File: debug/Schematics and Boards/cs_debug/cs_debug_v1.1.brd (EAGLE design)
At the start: 81.5 x 62.2 mm, 217 parts, among them J1 J-JTAG-CORTEX_SMD, J19 Solar, J3 HIROSE-DF40_50-PIN_CONNECTORS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, J5 J-WURTH-USBC, Q10 2N7002P, Q3 FDN340P, Q4 2N7002P, Q5 FDN340P, Q6 2N7002P, Q7 FDN340P, Q8 2N7002P, Q9 FDN340P, U1 AP2120N-3.3TRG1, U10 OPA357AIDBVTG4, U11 DAC7574IDGS, U12 MCP73871T-2CCI/ML, U13 USB2412-DZK, U14 INA225AIDGK, U15 OPA357AIDBVTG4, U2 TLV1117LV33DCYR, U204 LOADSWITCH-MIC94164, U3 ESD122DMYR, U5 INA225AIDGK, U6 OPA357AIDBVTG4, U7 INA225AIDGK, U8 OPA357AIDBVTG4, U9 INA225AIDGK, Y1 EPSON_TSX-3225_24.0000MF10Z-C3, Y101 32.768kHz, Y102 12MHz-12pF-K7

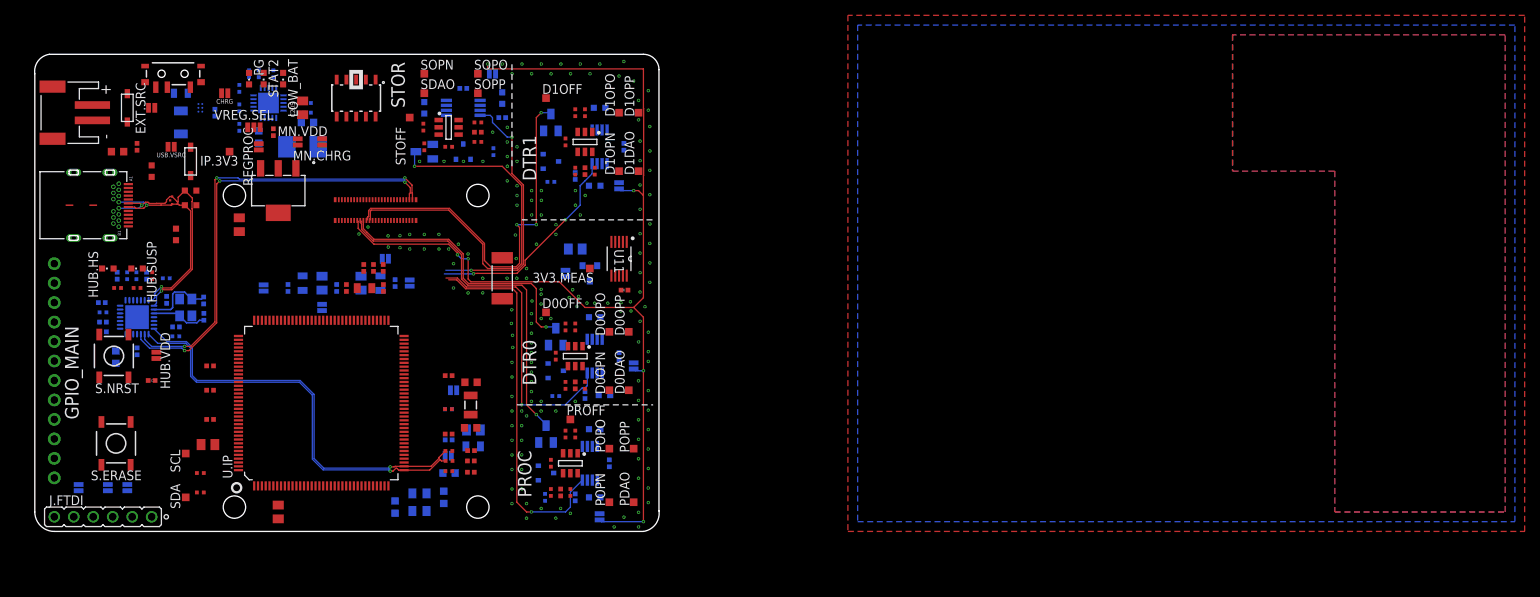
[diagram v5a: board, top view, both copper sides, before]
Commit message: Debug v1.1 board routed w/ 5 mil trace/space, 2 layer, 3.2x2.45in
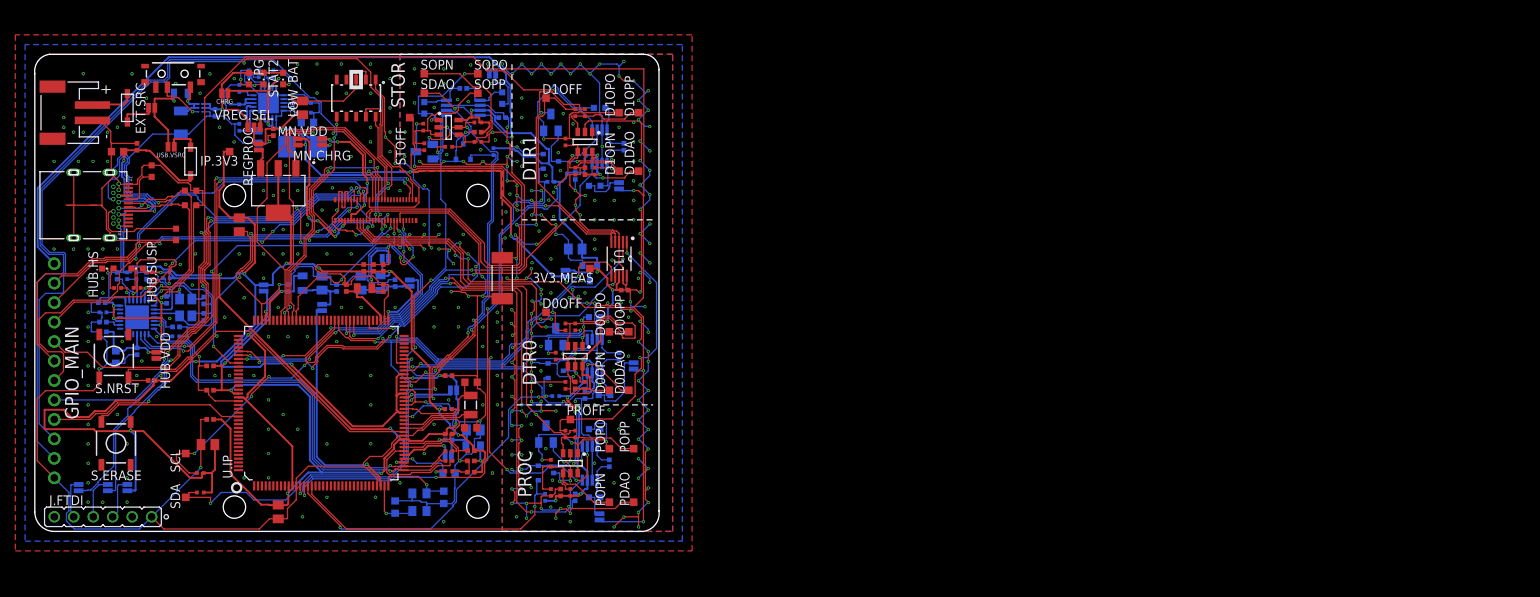
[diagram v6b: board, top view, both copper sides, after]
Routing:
- net DGND: track 0.00 -> 581.8 mm, vias 20 -> 174
- net AGND: track 0.00 -> 420.4 mm, vias 149 -> 232
- net 3V3_INSTR_MEAS: track 0.00 -> 212.1 mm, vias 0 -> 12
- net 3V3_INSTR_PROC: track 0.00 -> 197.7 mm, vias 0 -> 10
- net MAIN_TRACE_D3/GPIO16: track 0.00 -> 118.2 mm, vias 0 -> 1
- net VDDOUT: track 0.00 -> 113.7 mm, vias 0 -> 8
- net MAIN_TRACE_CLK/GPIO17: track 0.00 -> 105.0 mm, vias 0 -> 1
- net INSTR_PROC_I2C_SDA: track 0.00 -> 96.0 mm, vias 0 -> 3
- net CM_DTR1_DIFFAMP_GAIN0: track 0.00 -> 95.1 mm, vias 0 -> 3
- net USBC_VBUS: track 0.00 -> 90.8 mm, vias 0 -> 4
- net INSTR_PROC_I2C_SCL: track 0.00 -> 85.5 mm, vias 0 -> 6
- net VDDIO1: track 0.00 -> 74.7 mm, vias 0 -> 3
- net CM_DTR1_DCBIAS_SHUTDOWN: track 0.00 -> 73.9 mm, vias 0 -> 3
- net CM_STOR_DCBIAS_SHUTDOWN: track 0.00 -> 68.3 mm, vias 0 -> 3
- net MAIN_TRACE_D0/GPIO13: track 0.00 -> 65.5 mm, vias 0 -> 2
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
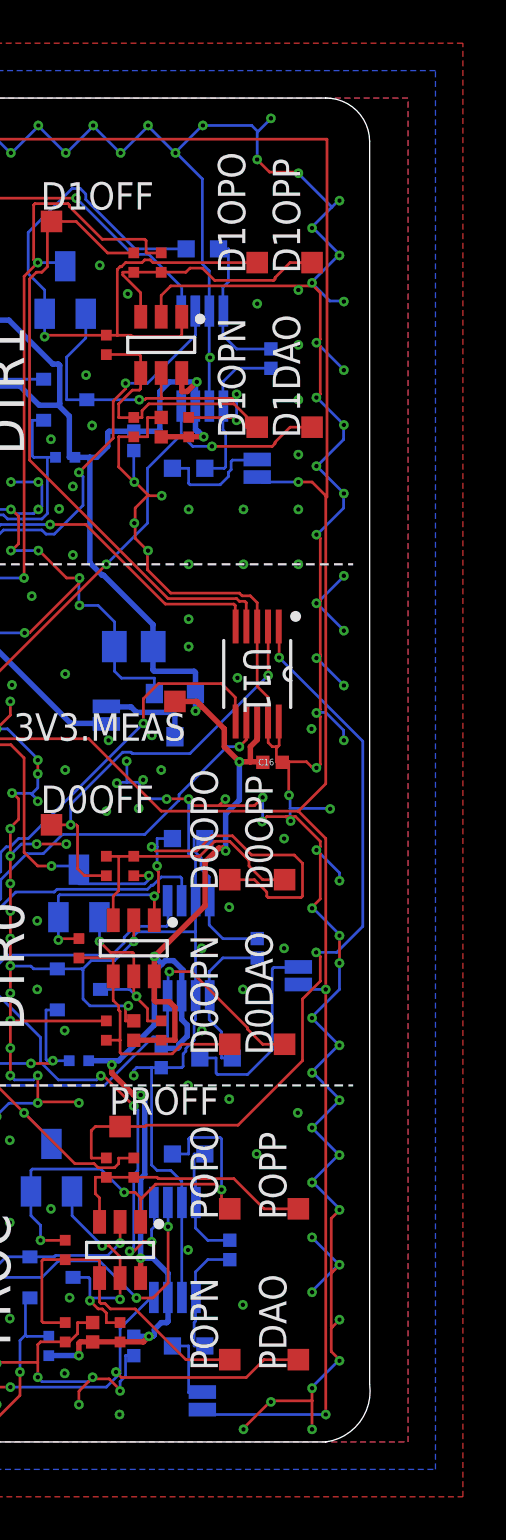
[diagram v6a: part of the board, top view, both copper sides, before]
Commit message: minor silk change
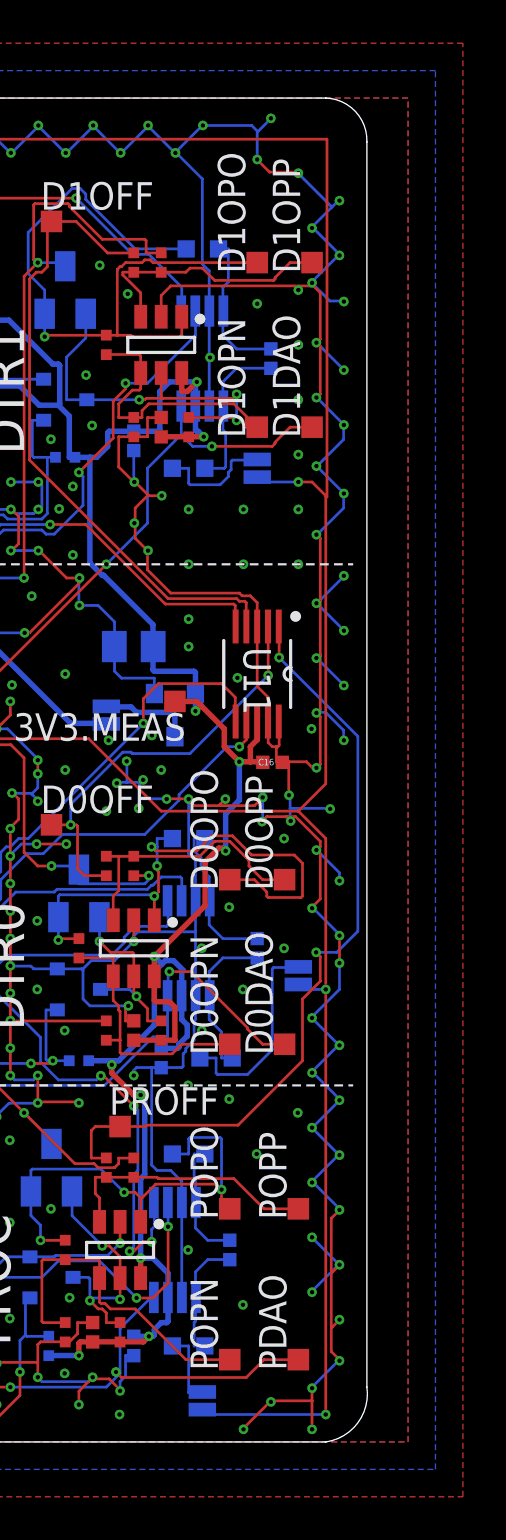
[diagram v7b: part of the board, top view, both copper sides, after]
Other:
- board size 81.5 x 62.2 mm -> 81.3 x 62.2 mm
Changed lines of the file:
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@@
 <plain>
 <wire x1="-20.32" y1="0" x2="56.515" y2="0" width="0" layer="20"/>
-<wire x1="58.547" y1="2.667" x2="58.547" y2="60.2234" width="0" layer="20"/>
+<wire x1="58.42" y1="2.54" x2="58.42" y2="60.198" width="0" layer="20"/>
 <wire x1="56.515" y1="62.23" x2="-20.955" y2="62.23" width="0" layer="20"/>
 <hole x="3.175" y="3.175" drill="2.921"/>
@@
 <text x="42.545" y="45.72" size="1.778" layer="25" rot="R90">DTR1</text>
 <text x="25.4" y="55.245" size="1.778" layer="25" rot="R90">STOR</text>
-<wire x1="56.515" y1="62.23" x2="58.547" y2="60.2234" width="0" layer="20" curve="-90"/>
+<wire x1="56.515" y1="62.23" x2="58.42" y2="60.198" width="0" layer="20" curve="-90"/>
 <wire x1="-22.86" y1="59.69" x2="-20.955" y2="62.23" width="0" layer="20" curve="-90"/>
 <wire x1="-22.86" y1="2.54" x2="-20.32" y2="0" width="0" layer="20" curve="90"/>
-<wire x1="56.515" y1="0" x2="58.547" y2="2.667" width="0" layer="20" curve="90"/>
+<wire x1="56.515" y1="0" x2="58.42" y2="2.54" width="0" layer="20" curve="90"/>
 <text x="-17.145" y="14.605" size="1.778" layer="21" rot="R90">GPIO_MAIN</text>
 </plain>
@@
 <wire x1="46.355" y1="13.1445" x2="46.355" y2="13.15" width="0.127" layer="1"/>
 <wire x1="54.356" y1="36.322" x2="54.356" y2="37.719" width="0.127" layer="1"/>
-<wire x1="58.2295" y1="32.4485" x2="54.356" y2="36.322" width="0.127" layer="16"/>
-<wire x1="58.2295" y1="23.876" x2="58.2295" y2="32.4485" width="0.127" layer="16"/>
-<wire x1="57.023" y1="22.6695" x2="58.2295" y2="23.876" width="0.127" layer="16"/>
+<wire x1="58.0009" y1="32.6771" x2="54.356" y2="36.322" width="0.127" layer="16"/>
+<wire x1="58.0009" y1="23.6474" x2="58.0009" y2="32.6771" width="0.127" layer="16"/>
+<wire x1="57.023" y1="22.6695" x2="58.0009" y2="23.6474" width="0.127" layer="16"/>
 <wire x1="56.0705" y1="22.6695" x2="57.023" y2="22.6695" width="0.127" layer="16"/>
 <wire x1="56.261" y1="22.479" x2="56.0705" y2="22.6695" width="0.127" layer="1"/>

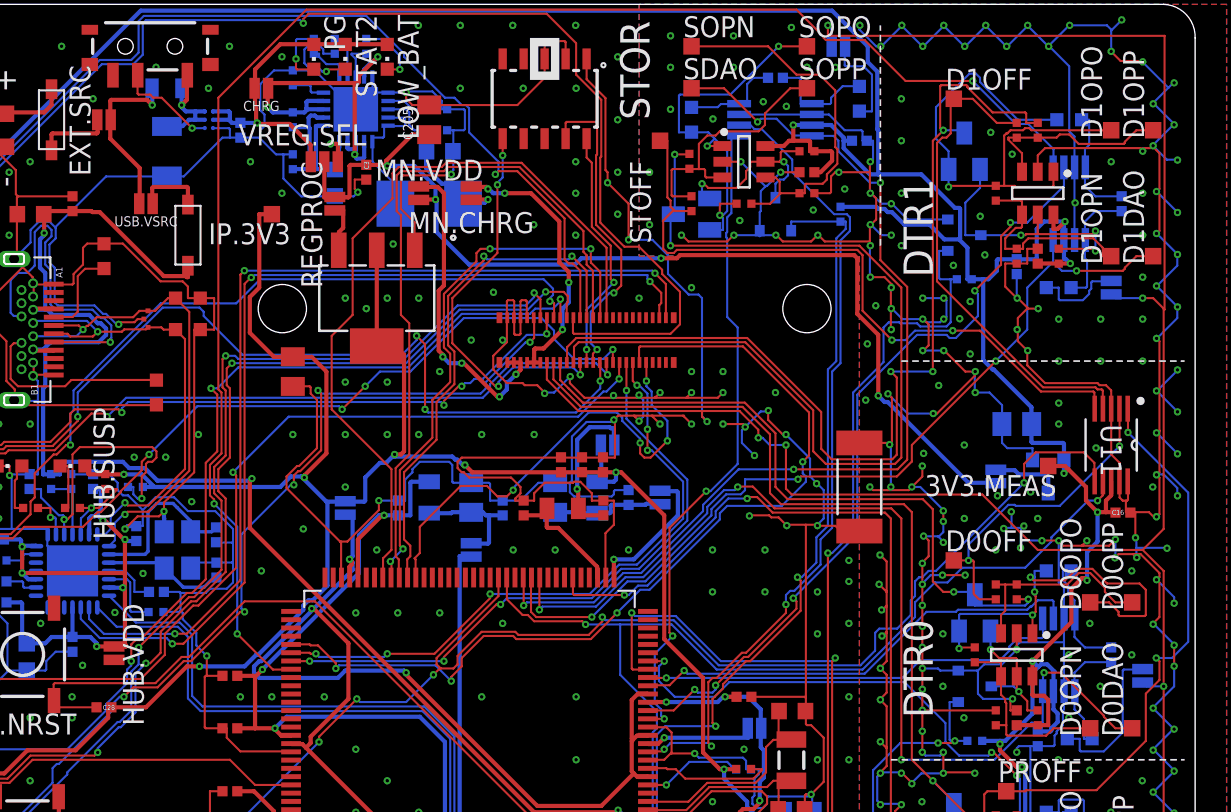
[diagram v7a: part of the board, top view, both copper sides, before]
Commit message: Minor changes, BOM generation & formatting, CAM for debug
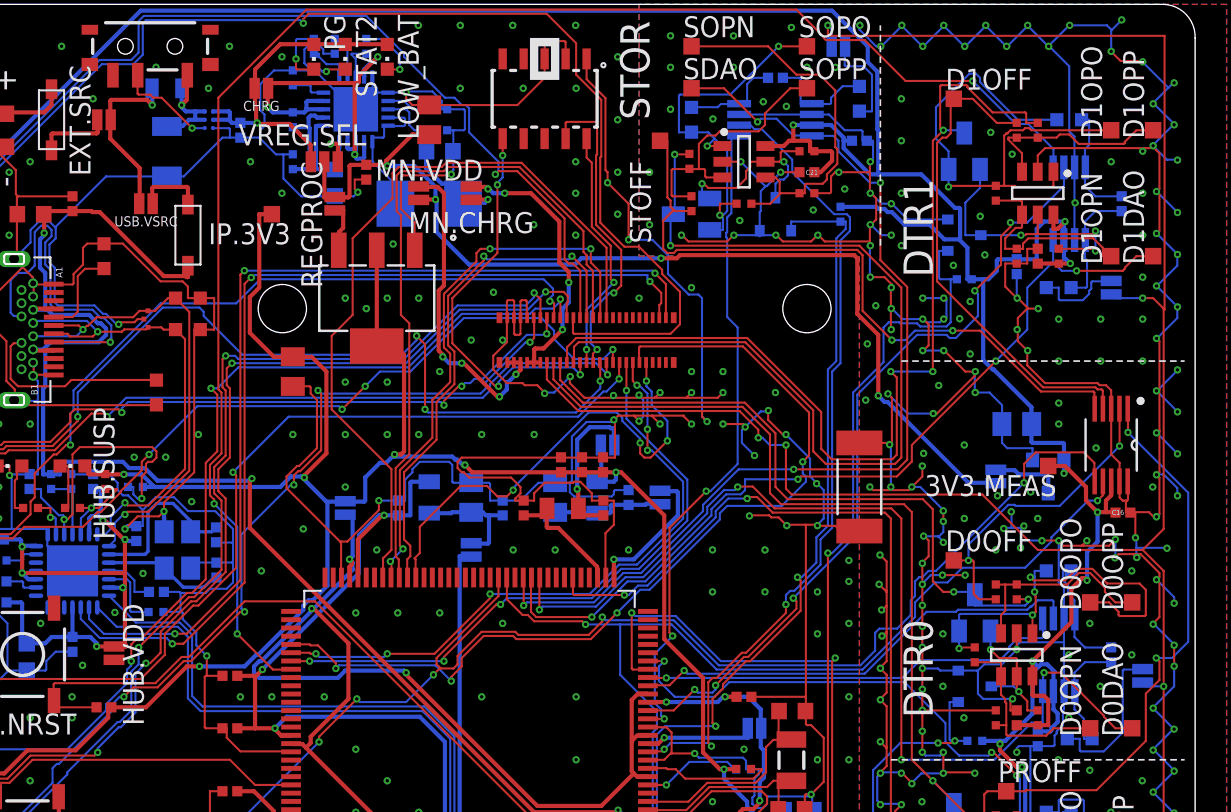
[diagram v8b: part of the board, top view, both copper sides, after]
